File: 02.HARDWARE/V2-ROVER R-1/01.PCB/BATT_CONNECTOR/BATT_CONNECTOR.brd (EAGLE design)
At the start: 21.8 x 18.1 mm, 15 parts, among them K1 FLEX11, Q1 DMG3415U-7

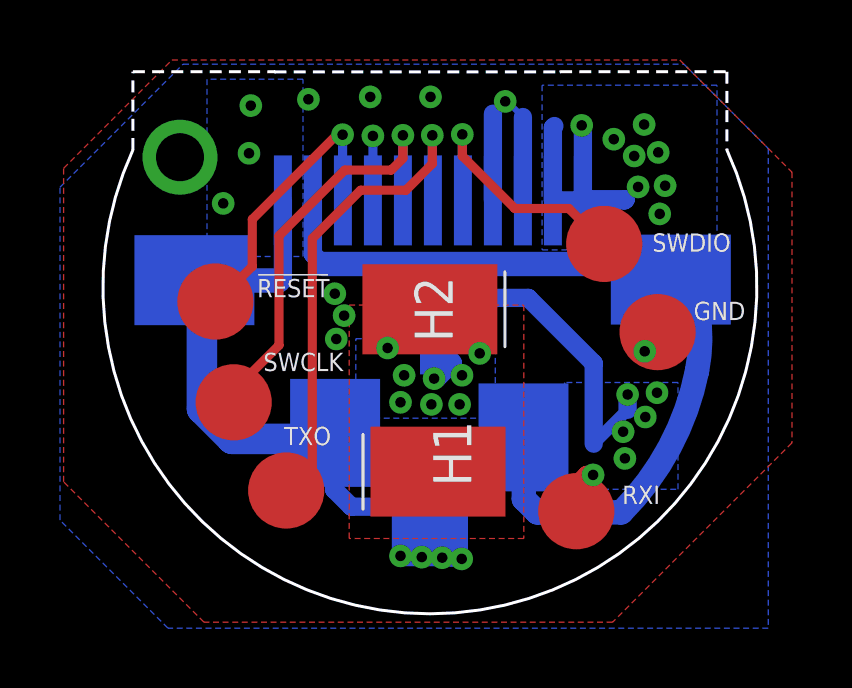
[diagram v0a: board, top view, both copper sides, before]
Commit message: Modificacion DCDC y Conector
DCDC: Posible version exclusiva PMU
Conector: Adatacion a cambio en produccion de un componente (SMJ)
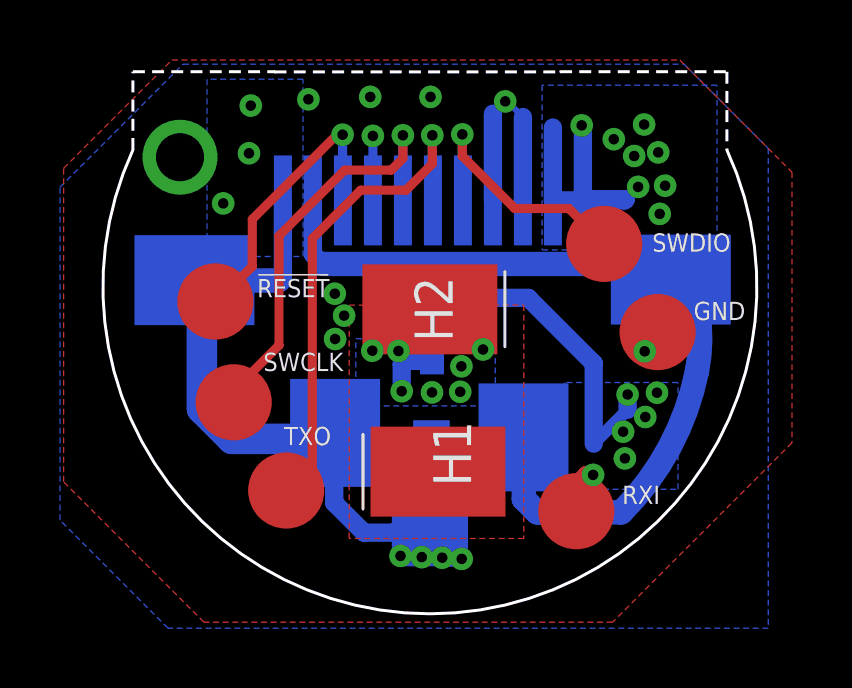
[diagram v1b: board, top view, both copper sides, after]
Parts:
- added D2: SM2T18A, SM2T18A:SM2T18A
- D1: value SM2T18A -> SMF16A; device SM2T18A:SM2T18A -> SMF16A:SODFL3618X110N
- moved D1 0.33 mm to (94.5, 85.7)
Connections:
- net VOUT+: now also D2.1
- net VOUT-: now also D2.2
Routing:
- net VOUT+: track 23.8 -> 25.8 mm
- net VBUS_IN: track 1.56 -> 1.96 mm, vias 8 -> 7

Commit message: Adiccion de Fiducidiales y actualizacion de Version
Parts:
- added FD_1, FD_2, FD_3, FD_4: FD_1, testpad:TP06SQ
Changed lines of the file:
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@@
 <layer number="2" name="Route2" color="16" fill="1" visible="no" active="yes"/>
 <layer number="15" name="Route15" color="23" fill="1" visible="no" active="yes"/>
-<layer number="16" name="Bottom" color="1" fill="1" visible="yes" active="yes"/>
+<layer number="16" name="Bottom" color="1" fill="1" visible="no" active="yes"/>
 <layer number="17" name="Pads" color="2" fill="1" visible="yes" active="yes"/>
 <layer number="18" name="Vias" color="2" fill="1" visible="yes" active="yes"/>
 <layer number="19" name="Unrouted" color="6" fill="1" visible="yes" active="yes"/>
 <layer number="20" name="Dimension" color="24" fill="1" visible="yes" active="yes"/>
-<layer number="21" name="tPlace" color="7" fill="1" visible="no" active="yes"/>
-<layer number="22" name="bPlace" color="7" fill="1" visible="yes" active="yes"/>
-<layer number="23" name="tOrigins" color="15" fill="1" visible="no" active="yes"/>
-<layer number="24" name="bOrigins" color="15" fill="1" visible="yes" active="yes"/>
-<layer number="25" name="tNames" color="7" fill="1" visible="no" active="yes"/>
-<layer number="26" name="bNames" color="7" fill="1" visible="yes" active="yes"/>
+<layer number="21" name="tPlace" color="7" fill="1" visible="yes" active="yes"/>
+<layer number="22" name="bPlace" color="7" fill="1" visible="no" active="yes"/>
+<layer number="23" name="tOrigins" color="15" fill="1" visible="yes" active="yes"/>
+<layer number="24" name="bOrigins" color="15" fill="1" visible="no" active="yes"/>
+<layer number="25" name="tNames" color="7" fill="1" visible="yes" active="yes"/>
+<layer number="26" name="bNames" color="7" fill="1" visible="no" active="yes"/>
 <layer number="27" name="tValues" color="7" fill="1" visible="no" active="yes"/>
 <layer number="28" name="bValues" color="7" fill="1" visible="no" active="yes"/>
@@
 <layer number="37" name="tTest" color="7" fill="1" visible="no" active="yes"/>
 <layer number="38" name="bTest" color="7" fill="1" visible="no" active="yes"/>
-<layer number="39" name="tKeepout" color="4" fill="11" visible="no" active="yes"/>
-<layer number="40" name="bKeepout" color="1" fill="11" visible="yes" active="yes"/>
-<layer number="41" name="tRestrict" color="4" fill="10" visible="no" active="yes"/>
-<layer number="42" name="bRestrict" color="1" fill="10" visible="yes" active="yes"/>
+<layer number="39" name="tKeepout" color="4" fill="11" visible="yes" active="yes"/>
+<layer number="40" name="bKeepout" color="1" fill="11" visible="no" active="yes"/>
+<layer number="41" name="tRestrict" color="4" fill="10" visible="yes" active="yes"/>
+<layer number="42" name="bRestrict" color="1" fill="10" visible="no" active="yes"/>
 <layer number="43" name="vRestrict" color="2" fill="10" visible="no" active="yes"/>
 <layer number="44" name="Drills" color="7" fill="1" visible="no" active="yes"/>
@@
 <layer number="49" name="Reference" color="7" fill="1" visible="no" active="yes"/>
 <layer number="50" name="dxf" color="7" fill="1" visible="no" active="no"/>
-<layer number="51" name="tDocu" color="7" fill="1" visible="no" active="yes"/>
-<layer number="52" name="bDocu" color="7" fill="1" visible="yes" active="yes"/>
+<layer number="51" name="tDocu" color="7" fill="1" visible="yes" active="yes"/>
+<layer number="52" name="bDocu" color="7" fill="1" visible="no" active="yes"/>
 <layer number="53" name="tGND_GNDA" color="7" fill="9" visible="no" active="no"/>
 <layer number="54" name="bGND_GNDA" color="1" fill="9" visible="no" active="no"/>
@@
 <attribute name="VALUE" x="94.43" y="85.35" locked="yes" size="1.27" layer="28" rot="MR90" align="center"/>
 </element>
+<element name="FD_1" library="testpad" library_urn="urn:adsk.eagle:library:385" package="TP06SQ" package3d_urn="urn:adsk.eagle:package:27952/1" value="FD_1" x="87.35" y="85.61" smashed="yes" rot="MR45">
+<attribute name="POPULARITY" value="0" x="87.505565625" y="85.468578125" size="1.778" layer="28" rot="MR45" display="off"/>
+<attribute name="TP_SIGNAL_NAME" value="" x="86.0029625" y="84.262959375" size="1" layer="38" rot="MR45"/>
+<attribute name="VALUE" x="87.2602" y="85.160984375" size="0.0254" layer="28" rot="MR45"/>
+</element>
+<element name="FD_2" library="testpad" library_urn="urn:adsk.eagle:library:385" package="TP06SQ" package3d_urn="urn:adsk.eagle:package:27952/1" value="FD_1" x="103" y="97.49" smashed="yes" rot="MR45">
+<attribute name="POPULARITY" value="0" x="103.2969875" y="97.20715625" size="1.778" layer="28" rot="MR45" display="off"/>
+<attribute name="TP_SIGNAL_NAME" value="" x="101.6529625" y="96.142959375" size="1" layer="38" rot="MR45"/>
+<attribute name="VALUE" x="102.9102" y="97.040984375" size="0.0254" layer="28" rot="MR45"/>
+</element>
+<element name="FD_3" library="testpad" library_urn="urn:adsk.eagle:library:385" package="TP06SQ" package3d_urn="urn:adsk.eagle:package:27952/1" value="FD_1" x="85.32" y="93.71" smashed="yes" rot="R45">
+<attribute name="POPULARITY" value="0" x="84.88159375" y="93.285734375" size="1.778" layer="27" rot="R45" display="off"/>
+<attribute name="TP_SIGNAL_NAME" value="" x="86.6670375" y="92.362959375" size="1" layer="37" rot="R45"/>
+<attribute name="VALUE" x="85.4098" y="93.260984375" size="0.0254" layer="27" rot="R45"/>
+</element>
+<element name="FD_4" library="testpad" library_urn="urn:adsk.eagle:library:385" package="TP06SQ" package3d_urn="urn:adsk.eagle:package:27952/1" value="FD_1" x="102.81" y="87.53" smashed="yes" rot="R45">
+<attribute name="POPULARITY" value="0" x="102.668578125" y="87.388578125" size="1.778" layer="27" rot="R45" display="off"/>
+<attribute name="TP_SIGNAL_NAME" value="" x="104.1570375" y="86.182959375" size="1" layer="37" rot="R45"/>
+<attribute name="VALUE" x="102.8998" y="87.080984375" size="0.0254" layer="27" rot="R45"/>
+</element>
 </elements>
